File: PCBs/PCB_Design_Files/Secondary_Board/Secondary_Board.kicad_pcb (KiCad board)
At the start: 4 copper layers, 40.3 x 57.1 mm, 54 parts, among them IC1 TLV2333IDGKR, IC2 320S14-U, J1 Conn_FFC_8pin, J2 Conn_01x08_Pin, Q1 2N3904, Q2 2N3904, Q3 MMBT3904, Q4 MMBT3904, Q5 2N7002, Q6 BSS84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

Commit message: secondary board connectors
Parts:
- removed BT1: Battery, Connector_JST:JST_PH_S2B-PH-K_1x02_P2.00mm_Horizontal
- removed J2: Conn_01x08_Pin, Connector_PinHeader_2.54mm:PinHeader_1x08_P2.54mm_Vertical
- added BT2: Battery_Cell, Project Footprints:bat_pads, B.Cu at (126.5, 96.5)
- added J4: Conn_01x10_Pin, Connector_PinHeader_2.54mm:PinHeader_1x10_P2.54mm_Vertical, F.Cu at (109.7, 93.8)
- IC1: value TLV2333IDGKR -> SOP65P490X110-8N
- J1: value Conn_FFC_8pin -> 5034801000; footprint Project Footprints:Conn_FFC_8pin -> Project Footprints:Conn_FFC_10pin
- Q5, Q7: value 2N7002 -> SOT95P240X111-3N
- Q6, Q8: value BSS84 -> SOT95P240X120-3N
- U7: value TLV9002 -> SOT_9002IDDFR_TEX
- moved J1 1.37 mm to (109.6, 64.5)
- moved L1 0.59 mm to (119.8, 89.9)
- moved R19 0.29 mm to (137.9, 50.8)
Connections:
- J1 pad 1: +3V3 -> +3.7V
- J1 pad 2: +5V -> +3V3
- J1 pad 3: MCU_Red -> +5V
- J1 pad 4: MCU_IR -> GND
- J1 pad 5: GND -> /PWM_Red
- J1 pad 6: /V_ptat -> /PWM_IR
- J1 pad 7: V_bandgap -> /OP_CTRL
- Q7 pad 3: V_bandgap -> /V_bandgap
- R14 pad 1: MCU_Red -> /PWM_Red
- R16 pad 1: MCU_IR -> /PWM_IR
- R19 pad 2: MCU_OPA_CTRL -> /OP_CTRL
- U7 pad 6: V_bandgap -> /V_bandgap
- U7 pad 7: V_bandgap -> /V_bandgap
- U8 pad 1: V_bandgap -> /V_bandgap
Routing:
- net V_bandgap: track 64.6 -> 0.00 mm, vias 4 -> 0
- net /V_bandgap: track 0.00 -> 56.7 mm, vias 0 -> 3
- net /OP_CTRL: track 0.00 -> 56.1 mm, vias 0 -> 4
- net +3.7V: track 17.9 -> 72.6 mm, vias 0 -> 1
- net MCU_Red: track 39.4 -> 0.00 mm
- net /PWM_Red: track 0.00 -> 36.3 mm
- net MCU_IR: track 33.2 -> 0.00 mm
- net /PWM_IR: track 0.00 -> 29.5 mm
- net /V_ptat: track 25.5 -> 18.6 mm
- net GND: track 44.7 -> 47.3 mm, vias 39 -> 41
- net +3V3: track 64.9 -> 66.5 mm
- net +5V: track 11.7 -> 12.9 mm
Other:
- board text added: "Vbg Vptat Gnd CTRL PwmIR PwmRed GND 5V 3v3 3v7"
- board text removed: "Gnd Vbandgap Vptat Gnd PwmIR PwmRed 5V 3v3"

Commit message: change ldo
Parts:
- removed Q4: MMBT3904, Project Footprints:SOT23_FAS
- added C9: 180p, Capacitor_SMD:C_0603_1608Metric, F.Cu at (132.3, 87.1)
- IC1: value SOP65P490X110-8N -> TLV2333IDGKR
- Q5, Q7: value SOT95P240X111-3N -> 2N7002
- Q6, Q8: value SOT95P240X120-3N -> BSS84
- U7: value SOT_9002IDDFR_TEX -> TLV9002
- moved Q3 5.28 mm to (135.3, 85.0)
- moved U2 3.31 mm to (128.1, 94.6)
- moved R12 2.52 mm to (132.2, 89.9), turned to 0 degrees
- moved C6 1.86 mm to (136.3, 88.6)
- moved C7 1.86 mm to (138.1, 88.6)
- moved R13 1.45 mm to (132.3, 92.2), turned to 180 degrees
- moved R1 1.39 mm to (118.8, 82.6)
- moved R2 1.39 mm to (116.5, 82.6)
- moved R11 1.04 mm to (131.4, 83.5), turned to 0 degrees
- moved C3 0.44 mm to (118.4, 86.8)
- moved L1 0.44 mm to (119.8, 90.3)
- moved C2 0.44 mm to (118.4, 85.1)
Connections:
- Q3 pad 2: Net-(Q3-E) -> +3V3
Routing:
- net Net-(U6-IN-): track 0.00 -> 6.07 mm
- net /Power Management/Vfb: track 0.00 -> 4.75 mm
- net +3V3: track 66.5 -> 70.0 mm
- net Net-(U6-OUT): track 0.00 -> 2.51 mm
- net Net-(Q3-B): track 0.08 -> 2.41 mm
- net +5V: track 12.9 -> 11.0 mm, vias 10 -> 9
- removed copper zone on F.Cu, net /Power Management/Vfb

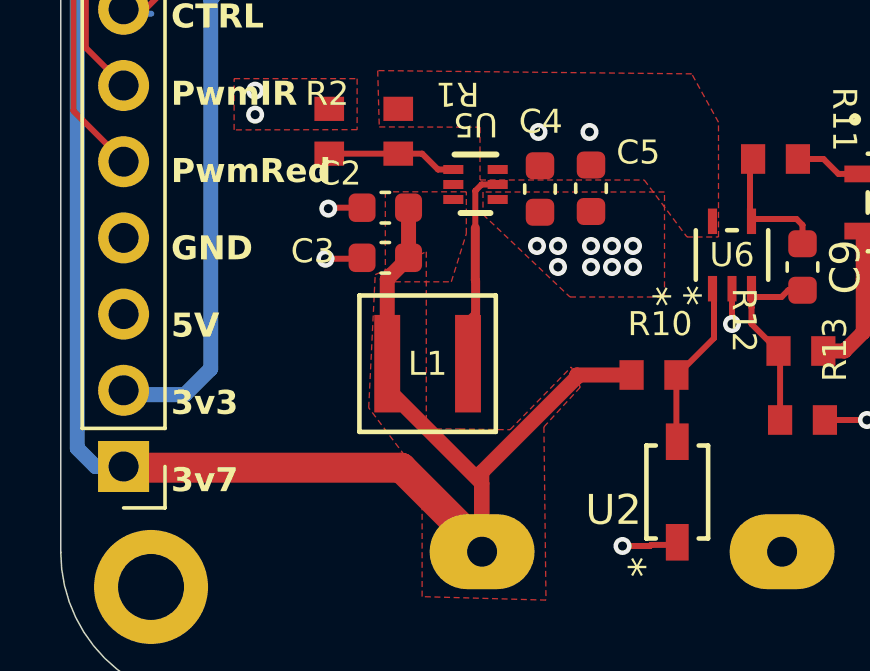
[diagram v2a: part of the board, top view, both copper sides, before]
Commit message: update inductor
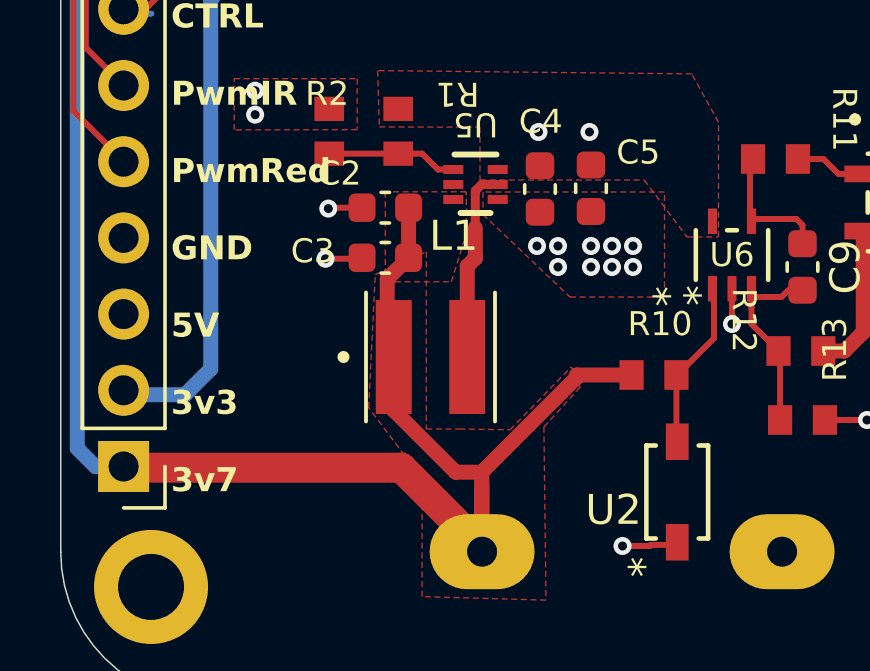
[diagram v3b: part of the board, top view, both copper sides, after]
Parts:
- L1: value XEL4030-102MEB -> VSEB0430H-1R0MC; footprint Project Footprints:IND_XEL4030_3.1_COC -> Project Footprints:IND_VSEB0430H-1R0MC
- moved L1 0.24 mm to (119.9, 90.1)
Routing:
- net Net-(U5-SW): track 4.95 -> 8.24 mm
- net +3.7V: track 72.6 -> 73.8 mm

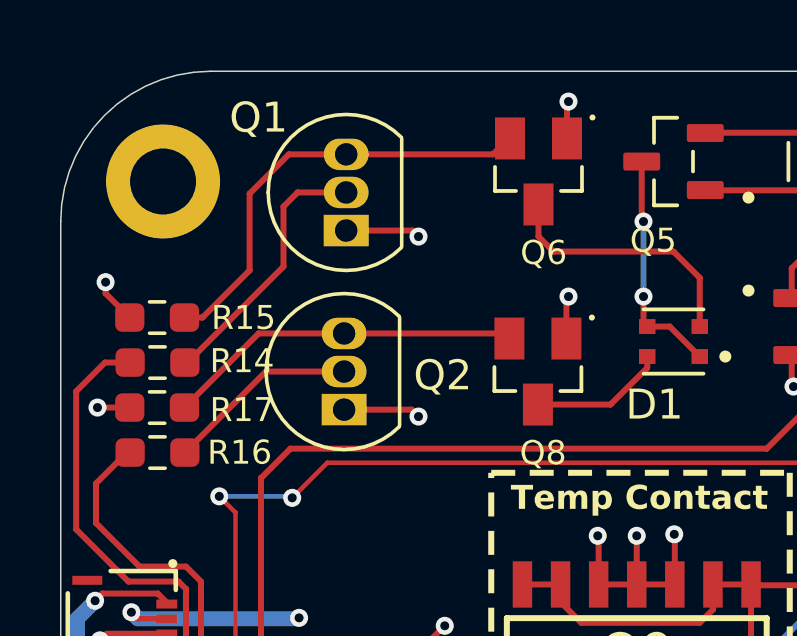
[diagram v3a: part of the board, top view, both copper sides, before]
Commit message: LED Driver updates
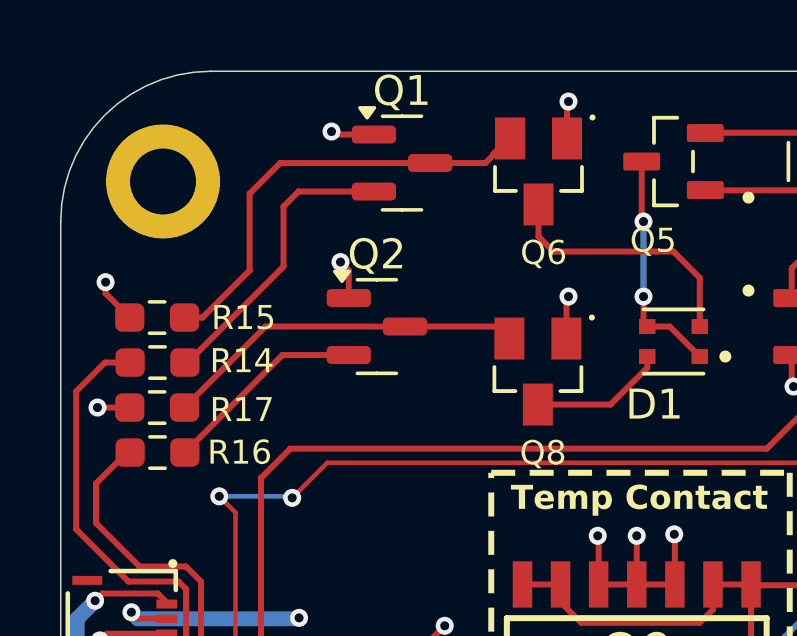
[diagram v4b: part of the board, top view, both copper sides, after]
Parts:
- Q1, Q2: value 2N3904 -> MMBT3904; footprint Package_TO_SOT_THT:TO-92_Inline -> Package_TO_SOT_SMD:SOT-23
- moved Q2 2.98 mm to (118.1, 53.0), turned to 0 degrees
- moved Q1 2.92 mm to (119.0, 47.5), turned to 0 degrees
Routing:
- net GND: track 47.2 -> 44.9 mm
- net Net-(Q1-B): track 8.90 -> 9.83 mm
- net Net-(Q1-C): track 14.8 -> 15.6 mm

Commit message: BOM updated
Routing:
- net Net-(U8--IN): track 11.8 -> 14.8 mm, vias 0 -> 2
- net GND: track 44.9 -> 47.1 mm
- net +5V: track 11.0 -> 9.72 mm, vias 9 -> 8
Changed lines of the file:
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@@
 	)
 	(segment
+		(start 133 46.54)
+		(end 133 45.6)
+		(width 0.2)
+		(layer "F.Cu")
+		(net 2)
+	)
+	(segment
 		(start 126.775 69.997)
 		(end 126.775 71.475)
@@
 	)
 	(segment
+		(start 133 45.6)
+		(end 132.75 45.35)
+		(width 0.2)
+		(layer "F.Cu")
+		(net 2)
+	)
+	(segment
 		(start 138.6292 74.9792)
 		(end 137.714109 74.9792)
@@
 	)
 	(segment
+		(start 131 45.35)
+		(end 130.85 45.5)
+		(width 0.2)
+		(layer "F.Cu")
+		(net 2)
+	)
+	(segment
 		(start 118.4281 75.5719)
 		(end 118.175 75.825)
@@
 	)
 	(segment
+		(start 132.75 45.35)
+		(end 131 45.35)
+		(width 0.2)
+		(layer "F.Cu")
+		(net 2)
+	)
+	(segment
 		(start 115.075 69.525)
 		(end 115.025 69.575)
@@
 	)
 	(segment
-		(start 133 46.54)
-		(end 133 45.5)
-		(width 0.2)
-		(layer "F.Cu")
-		(net 2)
-	)
-	(segment
 		(start 111.15 65.740008)
 		(end 112.213421 65.740008)
@@
 	)
 	(via
-		(at 133 45.5)
-		(size 0.6)
-		(drill 0.3)
-		(layers "F.Cu" "B.Cu")
-		(net 2)
-	)
-	(via
 		(at 136 49)
 		(size 0.6)
@@
 	)
 	(via
+		(at 130.85 45.5)
+		(size 0.6)
+		(drill 0.3)
+		(layers "F.Cu" "B.Cu")
+		(net 2)
+	)
+	(via
 		(at 126.65 86.4)
 		(size 0.6)
@@
 	)
 	(segment
-		(start 124.45 46.73)
-		(end 124.45 45.55)
-		(width 0.2)
-		(layer "F.Cu")
-		(net 21)
-	)
-	(segment
 		(start 136.42725 84.95)
 		(end 136.42225 84.945)
@@
 	)
 	(segment
-		(start 124.45 45.55)
-		(end 124.5 45.5)
-		(width 0.2)
-		(layer "F.Cu")
-		(net 21)
-	)
-	(segment
 		(start 109.07 51.895)
 		(end 109.875 52.7)
@@
 	)
 	(via
-		(at 124.5 45.5)
-		(size 0.6)
-		(drill 0.3)
-		(layers "F.Cu" "B.Cu")
-		(net 21)
-	)
-	(via
 		(at 109.07 51.52)
 		(size 0.6)
@@
 	)
 	(segment
-		(start 129.07 46.54)
-		(end 129.06 46.55)
+		(start 131.528 50.028)
+		(end 137.797 50.028)
 		(width 0.2)
 		(layer "F.Cu")
@@
 	)
 	(segment
-		(start 132.35 47.35)
-		(end 132.5 47.5)
+		(start 132.35 46.54)
+		(end 129.07 46.54)
 		(width 0.2)
 		(layer "F.Cu")
@@
 	)
 	(segment
-		(start 138.25 47.5)
-		(end 138.825 48.075)
+		(start 130.9 49.4)
+		(end 131.528 50.028)
 		(width 0.2)
 		(layer "F.Cu")
@@
 	)
 	(segment
-		(start 132.35 46.54)
-		(end 132.35 47.35)
+		(start 129.07 46.54)
+		(end 129.06 46.55)
 		(width 0.2)
 		(layer "F.Cu")
@@
 	)
 	(segment
-		(start 132.5 47.5)
-		(end 138.25 47.5)
+		(start 137.797 50.028)
+		(end 138.825 49)
 		(width 0.2)
 		(layer "F.Cu")
 		(net 30)
 	)
+	(via
+		(at 130.85 46.54)
+		(size 0.6)
+		(drill 0.3)
+		(layers "F.Cu" "B.Cu")
+		(net 30)
+	)
+	(via
+		(at 130.9 49.4)
+		(size 0.6)
+		(drill 0.3)
+		(layers "F.Cu" "B.Cu")
+		(net 30)
+	)
 	(segment
-		(start 132.35 46.54)
-		(end 129.07 46.54)
+		(start 130.85 46.54)
+		(end 130.85 49.35)
 		(width 0.2)
-		(layer "F.Cu")
+		(layer "B.Cu")
 		(net 30)
 	)
 	(segment
-		(start 138.825 48.075)
-		(end 138.825 49)
+		(start 130.85 49.35)
+		(end 130.9 49.4)
 		(width 0.2)
-		(layer "F.Cu")
+		(layer "B.Cu")
 		(net 30)
 	)
@@
 	(segment
 		(start 131.94 52.05)
-		(end 131.94 51.06)
+		(end 131.94 51.16)
 		(width 0.2)
 		(layer "F.Cu")
@@
 	)
 	(segment
-		(start 131.94 51.06)
-		(end 132.5 50.5)
+		(start 131.94 51.16)
+		(end 132.31 50.79)
 		(width 0.2)
 		(layer "F.Cu")
@@
 	)
 	(segment
-		(start 132.5 50.5)
-		(end 137 50.5)
+		(start 132.31 50.79)
+		(end 136.9975 50.79)
 		(width 0.2)
 		(layer "F.Cu")
@@
 	)
 	(zone
-		(net 15)
-		(net_name "Net-(U5-SW)")
-		(layer "F.Cu")
-		(name "$teardrop_padvia$")
-		(hatch full 0.1)
-		(priority 30000)
-		(attr
-			(teardrop
-				(type padvia)
-			)
-		)
-		(connect_pads yes
-			(clearance 0)
-		)
-		(min_thickness 0.0254)
-		(filled_areas_thickness no)
-		(fill yes
-			(thermal_gap 0.5)
-			(thermal_bridge_width 0.5)
-			(island_removal_mode 1)
-			(island_area_min 10)
-		)
-		(polygon
-			(pts
-				(xy 121.375 87.6) (xy 120.875 87.6) (xy 120.525 88.2) (xy 121.125 90.101) (xy 121.725 88.2)
-			)
-		)
-	)
-	(zone
 		(net 14)
 		(net_name "+3.7V")
@@
 			)
 		)
+	)
+	(zone
+		(net 15)
+		(net_name "Net-(U5-SW)")
+		(layer "F.Cu")
+		(name "$teardrop_padvia$")
+		(hatch full 0.1)
+		(priority 30000)
+		(attr
+			(teardrop
+				(type padvia)
+			)
+		)
+		(connect_pads yes
+			(clearance 0)
+		)
+		(min_thickness 0.0254)
+		(filled_areas_thickness no)
+		(fill yes
+			(thermal_gap 0.5)
+			(thermal_bridge_width 0.5)
+			(island_removal_mode 1)
+			(island_area_min 10)
+		)
+		(polygon
+			(pts
+				(xy 121.375 87.6) (xy 120.875 87.6) (xy 120.525 88.2) (xy 121.125 90.101) (xy 121.725 88.2)
+			)
+		)

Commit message: final checks
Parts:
- IC1: value TLV2333IDGKR -> SOP65P490X110-8N
- Q5, Q7: value 2N7002 -> SOT95P240X111-3N
- Q6, Q8: value BSS84 -> SOT95P240X120-3N
- U7: value TLV9002 -> SOT_9002IDDFR_TEX
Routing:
- net GND: track 47.1 -> 50.2 mm, vias 41 -> 42
- net +5V: track 9.72 -> 11.2 mm, vias 8 -> 9
- net +3.7V: track 73.8 -> 74.3 mm

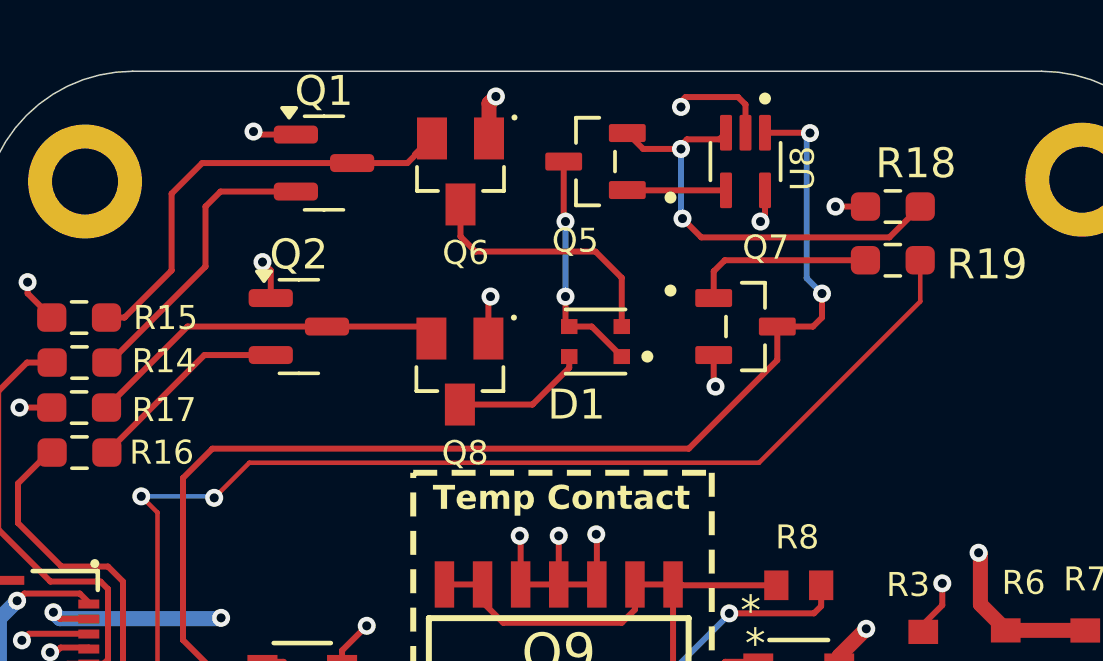
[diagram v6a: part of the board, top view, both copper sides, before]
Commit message: added pull up to bg led driver
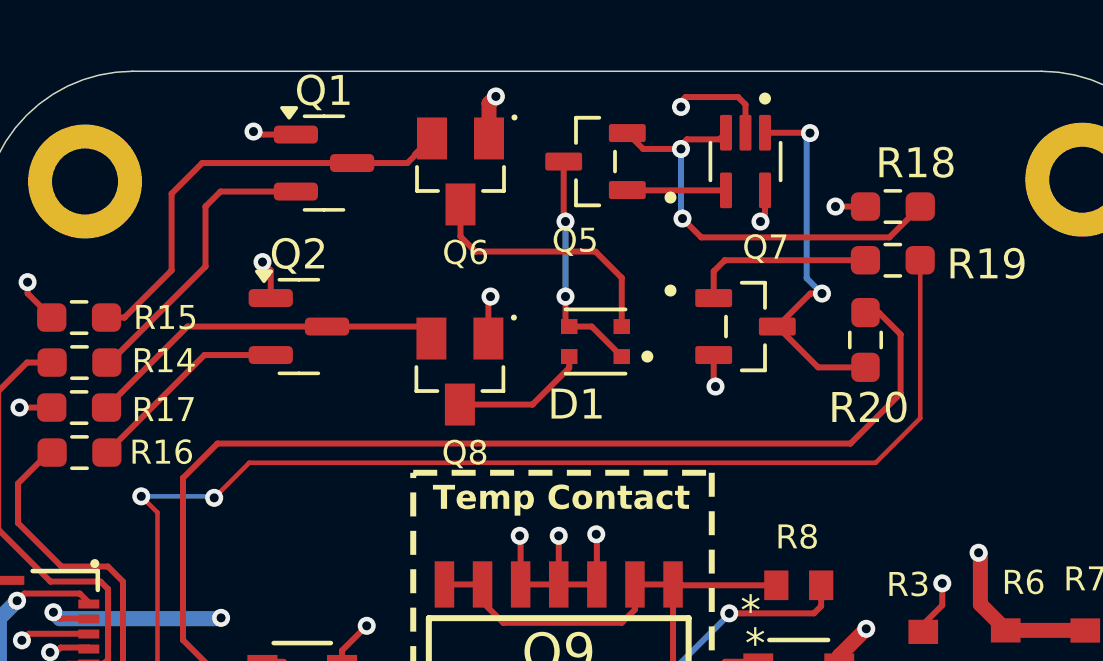
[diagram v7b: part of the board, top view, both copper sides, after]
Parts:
- added R20: 10k, Resistor_SMD:R_0603_1608Metric_Pad0.98x0.95mm_HandSolder, F.Cu at (137.0, 53.4)
- IC1: value SOP65P490X110-8N -> TLV2333IDGKR
- Q5, Q7: value SOT95P240X111-3N -> 2N7002
- Q6, Q8: value SOT95P240X120-3N -> BSS84
- U7: value SOT_9002IDDFR_TEX -> TLV9002
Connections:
- Q7 pad 3: /V_bandgap -> Net-(U8-+IN)
- U8 pad 1: /V_bandgap -> Net-(U8-+IN)
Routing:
- net Net-(U8-+IN): track 0.00 -> 12.6 mm, vias 0 -> 2
- net /V_bandgap: track 56.7 -> 53.1 mm, vias 3 -> 1
- net /OP_CTRL: track 56.1 -> 58.4 mm
